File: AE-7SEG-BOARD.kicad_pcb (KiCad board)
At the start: 2 copper layers, 12 x 25.5 mm, 16 parts, among them U1 74HC595D, 118, U2 7-SEGMENT-LED

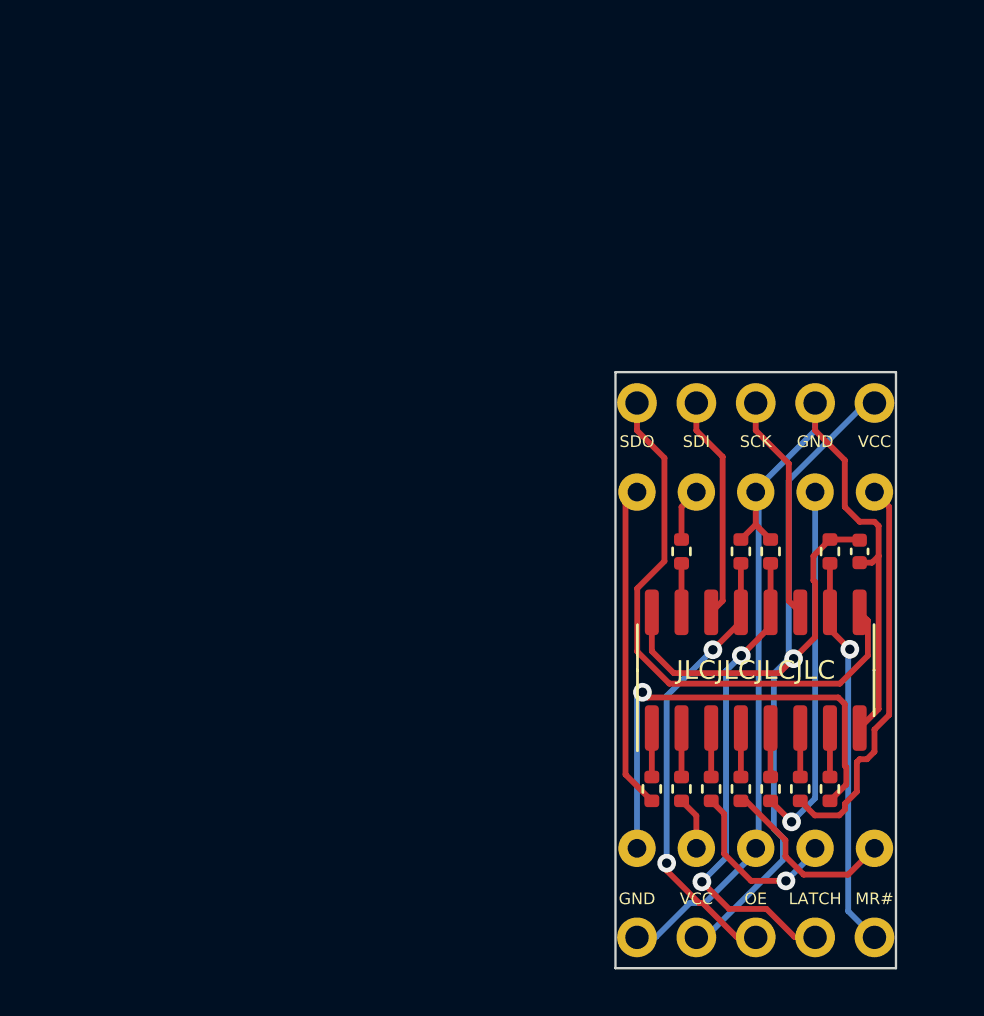
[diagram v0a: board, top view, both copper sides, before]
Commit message: Update KiCAD 7.0
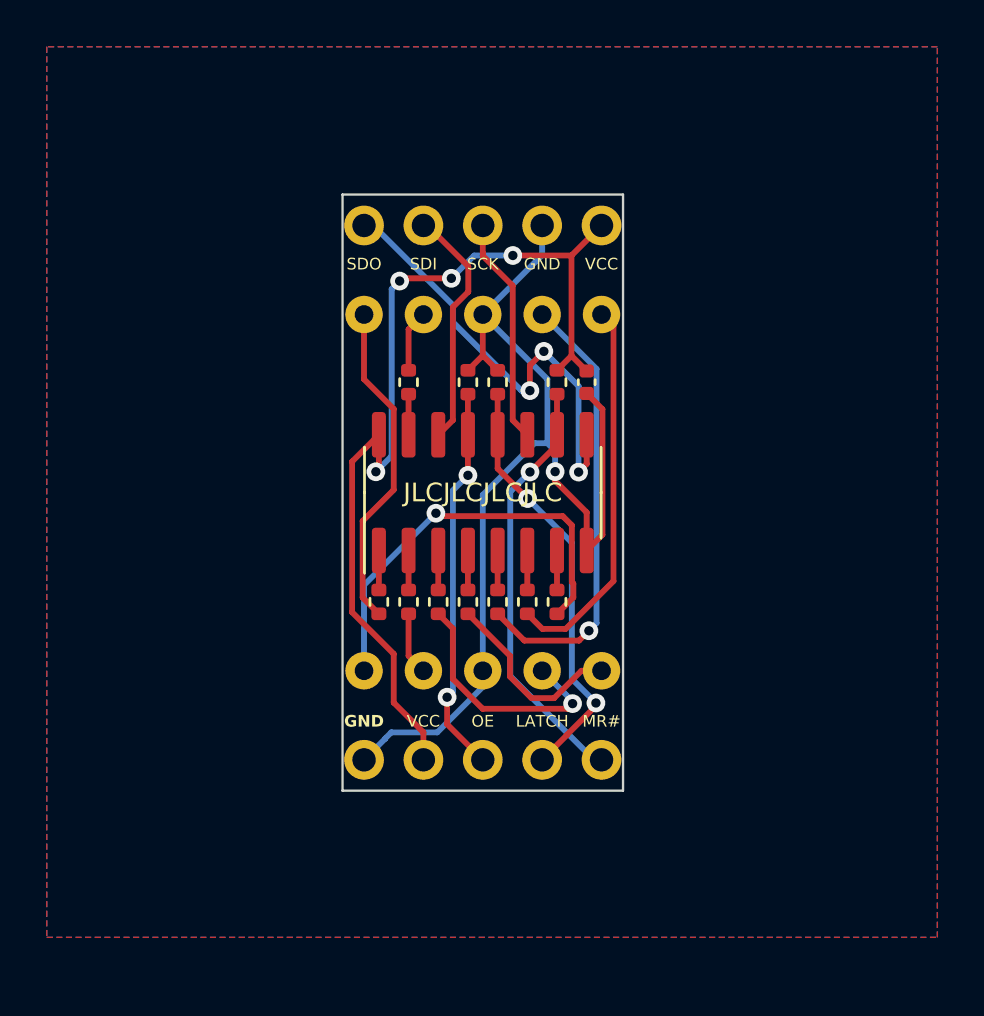
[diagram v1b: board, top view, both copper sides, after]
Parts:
- moved R3 14.2 mm to (142.5, 112.6)
- moved R4 14.2 mm to (143.7, 112.6)
- moved R6 14.2 mm to (146.3, 112.6)
- moved R7 14.2 mm to (147.6, 112.6)
- moved R2 14.2 mm to (141.2, 112.6)
- moved R5 14.2 mm to (145.0, 112.6)
- moved R8 14.2 mm to (148.8, 112.6)
- moved U1 13.9 mm to (145.7, 108.0)
- moved CH1 13.9 mm to (150.7, 96.5)
- moved CH2 13.9 mm to (150.7, 119.4)
- moved U2 13.9 mm to (150.7, 115.6)
- moved C1 13.7 mm to (150.1, 103.3)
- moved R1 13.7 mm to (142.5, 103.3)
- moved R10 13.7 mm to (146.3, 103.3)
- moved R11 13.7 mm to (145.0, 103.3)
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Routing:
- net /SDO: track 24.5 -> 19.9 mm, vias 0 -> 3
- net Net-(U2-F): track 15.8 -> 19.2 mm
- net Net-(U2-D): track 7.53 -> 10.7 mm
- net /OE: track 19.4 -> 16.6 mm
- net /LATCH: track 20.6 -> 18.3 mm
- net Net-(U2-DP): track 20.1 -> 18.1 mm
- net /MR#: track 16.8 -> 18.3 mm
- net GND: track 46.8 -> 45.9 mm, vias 0 -> 1
- net VCC: track 42.5 -> 41.6 mm, vias 1 -> 4
- net /SDI: track 9.62 -> 10.4 mm
- net Net-(U2-G): track 17.1 -> 16.4 mm
- added copper zone on B.Cu, net GND
- added copper zone on F.Cu, net GND
